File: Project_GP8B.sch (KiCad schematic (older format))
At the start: 15 parts, among them U1 74AHC05, U2 74AHC05, U3 74AHC1G04, U4 74AHC1G04, U5 74AHC05

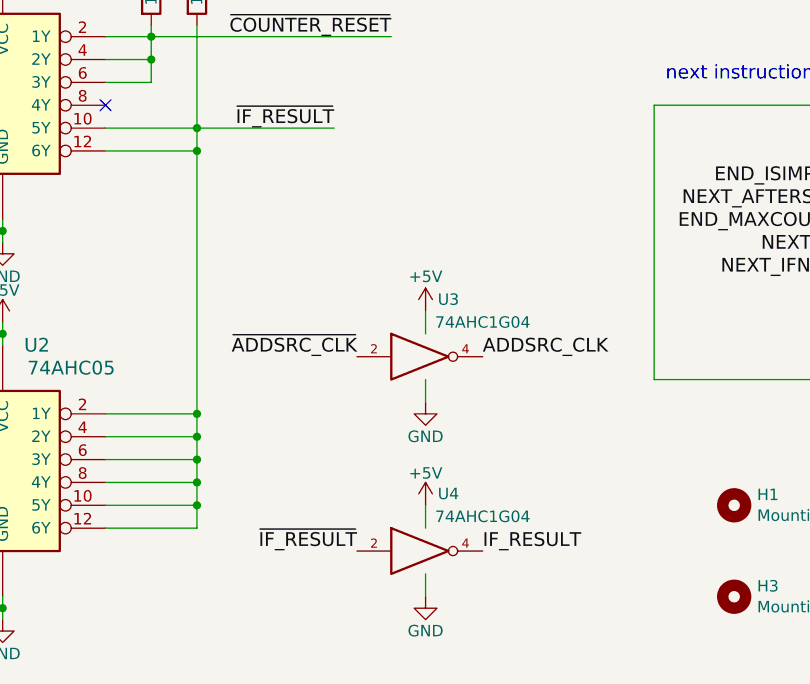
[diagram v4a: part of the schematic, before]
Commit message: Apply MM1 memory standard, and shared power pin symbol fix
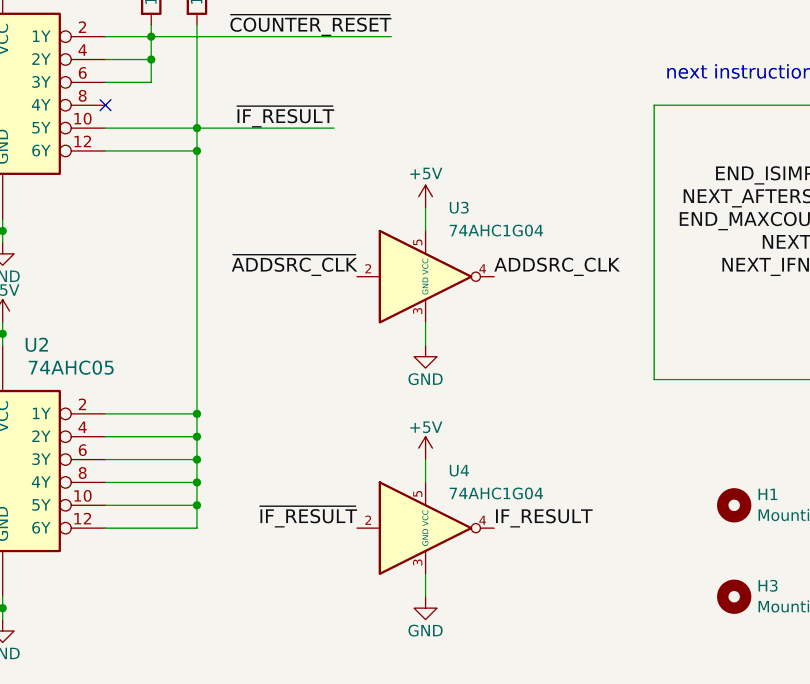
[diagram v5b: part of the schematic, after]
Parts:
- removed U3, U4: 74AHC1G04, Package_TO_SOT_SMD:SOT-23-5, symbol 74xGxx:74AHC1G04
- added U3, U4: 74AHC1G04, Package_TO_SOT_SMD:SOT-23-5, symbol Custom:74AHC1G04
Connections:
- net +5V: now also U3.5 (VCC), U4.5 (VCC)
- net ADDSRC_CLK: now also U3.4
- net GND: now also U3.3 (GND), U4.3 (GND)
- net IF_RESULT: now also U4.4
- net ~ADDSRC_CLK: now also U3.2
- net ~IF_RESULT: now also U4.2
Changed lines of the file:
@@
 L power:+5V #PWR07
 U 1 1 5B155C11
-P 3700 6150
-F 0 "#PWR07" H 3700 6000 50  0001 C CNN
-F 1 "+5V" H 3700 6300 50  0000 C CNN
-F 2 "" H 3700 6150 50  0001 C CNN
-F 3 "" H 3700 6150 50  0001 C CNN
-	1    3700 6150
+P 3700 5700
+F 0 "#PWR07" H 3700 5550 50  0001 C CNN
+F 1 "+5V" H 3700 5850 50  0000 C CNN
+F 2 "" H 3700 5700 50  0001 C CNN
+F 3 "" H 3700 5700 50  0001 C CNN
+	1    3700 5700
 	1    0    0    -1
 $EndComp
@@
 L power:+5V #PWR08
 U 1 1 5B15C5EC
-P 3700 7000
-F 0 "#PWR08" H 3700 6850 50  0001 C CNN
-F 1 "+5V" H 3700 7140 50  0000 C CNN
-F 2 "" H 3700 7000 50  0001 C CNN
-F 3 "" H 3700 7000 50  0001 C CNN
-	1    3700 7000
+P 3700 6800
+F 0 "#PWR08" H 3700 6650 50  0001 C CNN
+F 1 "+5V" H 3700 6940 50  0000 C CNN
+F 2 "" H 3700 6800 50  0001 C CNN
+F 3 "" H 3700 6800 50  0001 C CNN
+	1    3700 6800
 	1    0    0    -1
 $EndComp
@@
 L power:GND #PWR09
 U 1 1 5B15D182
-P 3700 6550
-F 0 "#PWR09" H 3700 6300 50  0001 C CNN
-F 1 "GND" H 3700 6400 50  0000 C CNN
-F 2 "" H 3700 6550 50  0001 C CNN
-F 3 "" H 3700 6550 50  0001 C CNN
-	1    3700 6550
+P 3700 6300
+F 0 "#PWR09" H 3700 6050 50  0001 C CNN
+F 1 "GND" H 3700 6150 50  0000 C CNN
+F 2 "" H 3700 6300 50  0001 C CNN
+F 3 "" H 3700 6300 50  0001 C CNN
+	1    3700 6300
 	1    0    0    -1
 $EndComp
@@
 	1    0    0    -1
 $EndComp
-Text Label 3400 7200 2    60   ~ 0
+Text Label 3400 7100 2    60   ~ 0
 ~IF_RESULT
-Text Label 3950 7200 0    60   ~ 0
+Text Label 4000 7100 0    60   ~ 0
 IF_RESULT
 Text Label 4900 800  2    60   ~ 0
@@
 	1    0    0    -1
 $EndComp
-$Comp
-L 74xGxx:74AHC1G04 U3
-U 1 1 5C94A9C5
-P 3700 6350
-F 0 "U3" H 3800 6600 50  0000 C CNN
-F 1 "74AHC1G04" H 3950 6500 50  0000 C CNN
-F 2 "Package_TO_SOT_SMD:SOT-23-5" H 3700 6350 50  0001 C CNN
-F 3 "http://www.ti.com/lit/sg/scyt129e/scyt129e.pdf" H 3700 6350 50  0001 C CNN
-	1    3700 6350
-	1    0    0    -1
-$EndComp
-Wire Wire Line
-	3700 6150 3700 6250
-Wire Wire Line
-	3700 6450 3700 6550
-$Comp
-L 74xGxx:74AHC1G04 U4
-U 1 1 5C971EB2
-P 3700 7200
-F 0 "U4" H 3800 7450 50  0000 C CNN
-F 1 "74AHC1G04" H 3950 7350 50  0000 C CNN
-F 2 "Package_TO_SOT_SMD:SOT-23-5" H 3700 7200 50  0001 C CNN
-F 3 "http://www.ti.com/lit/sg/scyt129e/scyt129e.pdf" H 3700 7200 50  0001 C CNN
-	1    3700 7200
-	1    0    0    -1
-$EndComp
-Wire Wire Line
-	3700 7000 3700 7100
+Wire Wire Line
+	3700 5700 3700 5800
+Wire Wire Line
+	3700 6200 3700 6300
+Wire Wire Line
+	3700 6800 3700 6900
 Wire Wire Line
 	3700 7300 3700 7400
@@
 Text Label 7250 5600 2    60   ~ 0
 ~ADDSRC_CLK
-Text Label 3400 6350 2    60   ~ 0
+Text Label 3400 6000 2    60   ~ 0
 ~ADDSRC_CLK
-Text Label 3950 6350 0    60   ~ 0
+Text Label 4000 6000 0    60   ~ 0
 ADDSRC_CLK
 $Sheet
@@
 F23 "SPI_CS" I L 1400 2350 60
 $EndSheet
+$Comp
+L Custom:74AHC1G04 U4
+U 1 1 5F3E18E2
+P 3700 7100
+F 0 "U4" H 3800 7350 50  0000 L CNN
+F 1 "74AHC1G04" H 3800 7250 50  0000 L CNN
+F 2 "Package_TO_SOT_SMD:SOT-23-5" H 3700 7100 50  0001 C CNN
+F 3 "https://assets.nexperia.com/documents/data-sheet/74AHC_AHCT1G04.pdf" H 3700 7100 50  0001 C CNN
+	1    3700 7100
+	1    0    0    -1
+$EndComp
+$Comp
+L Custom:74AHC1G04 U3
+U 1 1 5F3E1C89
+P 3700 6000
+F 0 "U3" H 3800 6300 50  0000 L CNN
+F 1 "74AHC1G04" H 3800 6200 50  0000 L CNN
+F 2 "Package_TO_SOT_SMD:SOT-23-5" H 3700 6000 50  0001 C CNN
+F 3 "https://assets.nexperia.com/documents/data-sheet/74AHC_AHCT1G04.pdf" H 3700 6000 50  0001 C CNN
+	1    3700 6000
+	1    0    0    -1
+$EndComp
 Wire Bus Line
 	1700 2800 1700 3600

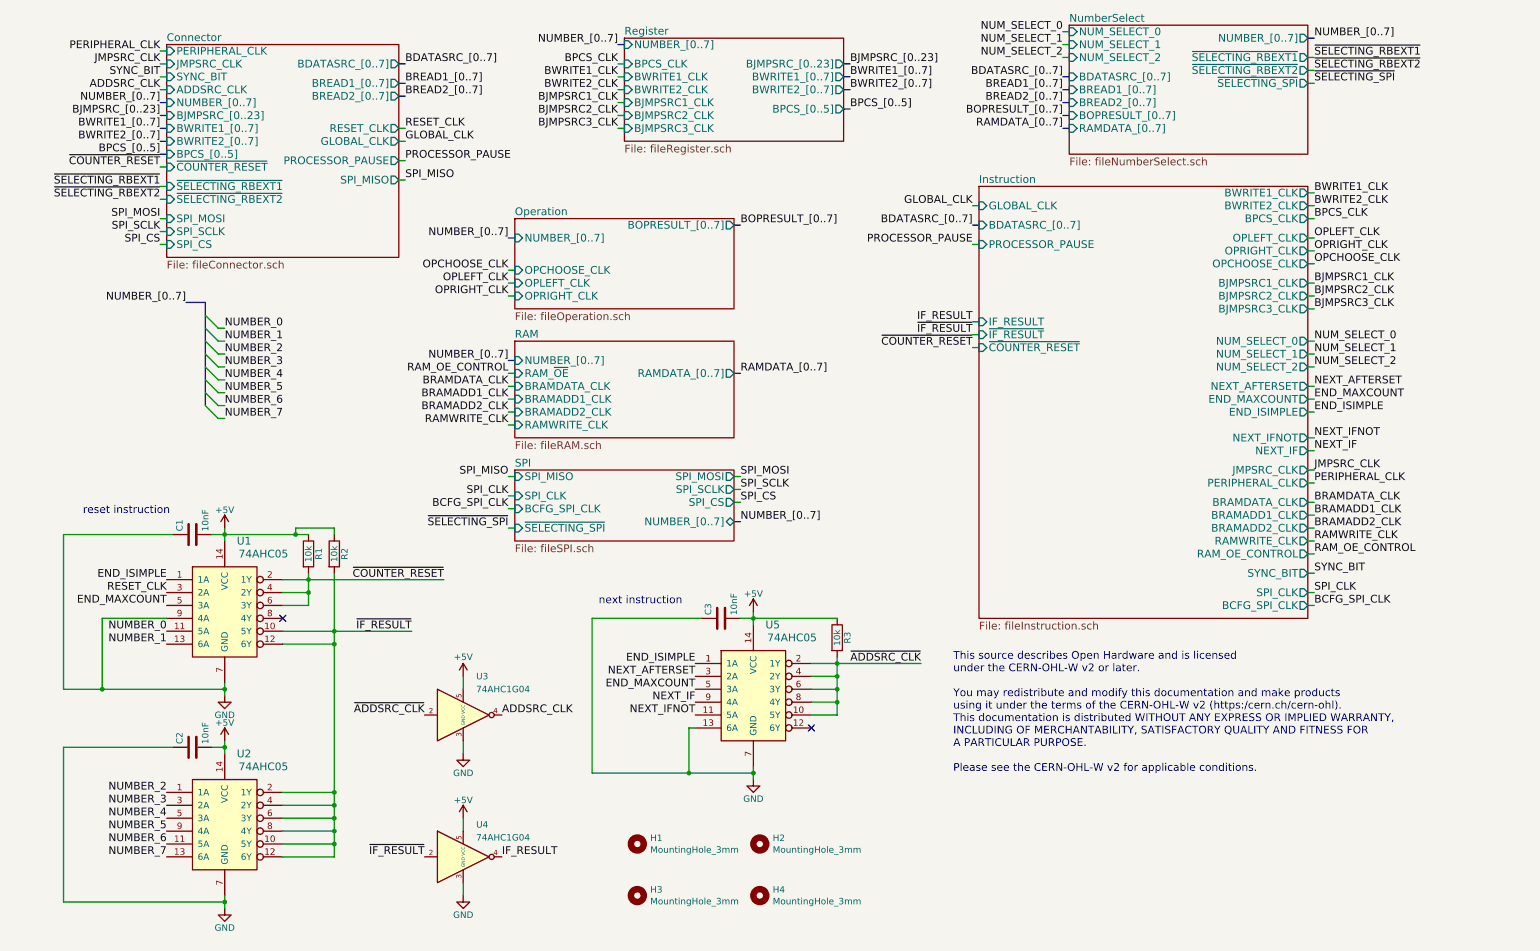
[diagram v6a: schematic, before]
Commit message: V5.1 (#9)
* Apply new symbol for XC2C256-VQ100 #5

* Set new date and 5.1

* Replacing 74HC165 with 74HC166, and add SPI_CFG_DS #4

* Replace some gates with a 74AHC1G02 to fix the pulse problem #3

* Go next only if SRCVALUE, (simple instruction)

* Remove weird ghost bus in register

* Small cleaning in fileRegister

* Go next only if SRCVALUE, (complex instruction) #8
adding 74AHC1G08

* Better decoupling #6

* Component association (#7)

* netlist

* Updated BOM for V5.1

* Routing, cleaning first pass

* bit of pcb cleaning

* SolderMaskClearance to 0

* Schematics to pdf

* PCB files in pdf

* exporting Gerbert files

* new 3d images

* Update README.md

* Modifying CHANGELOG file

* Update README.md
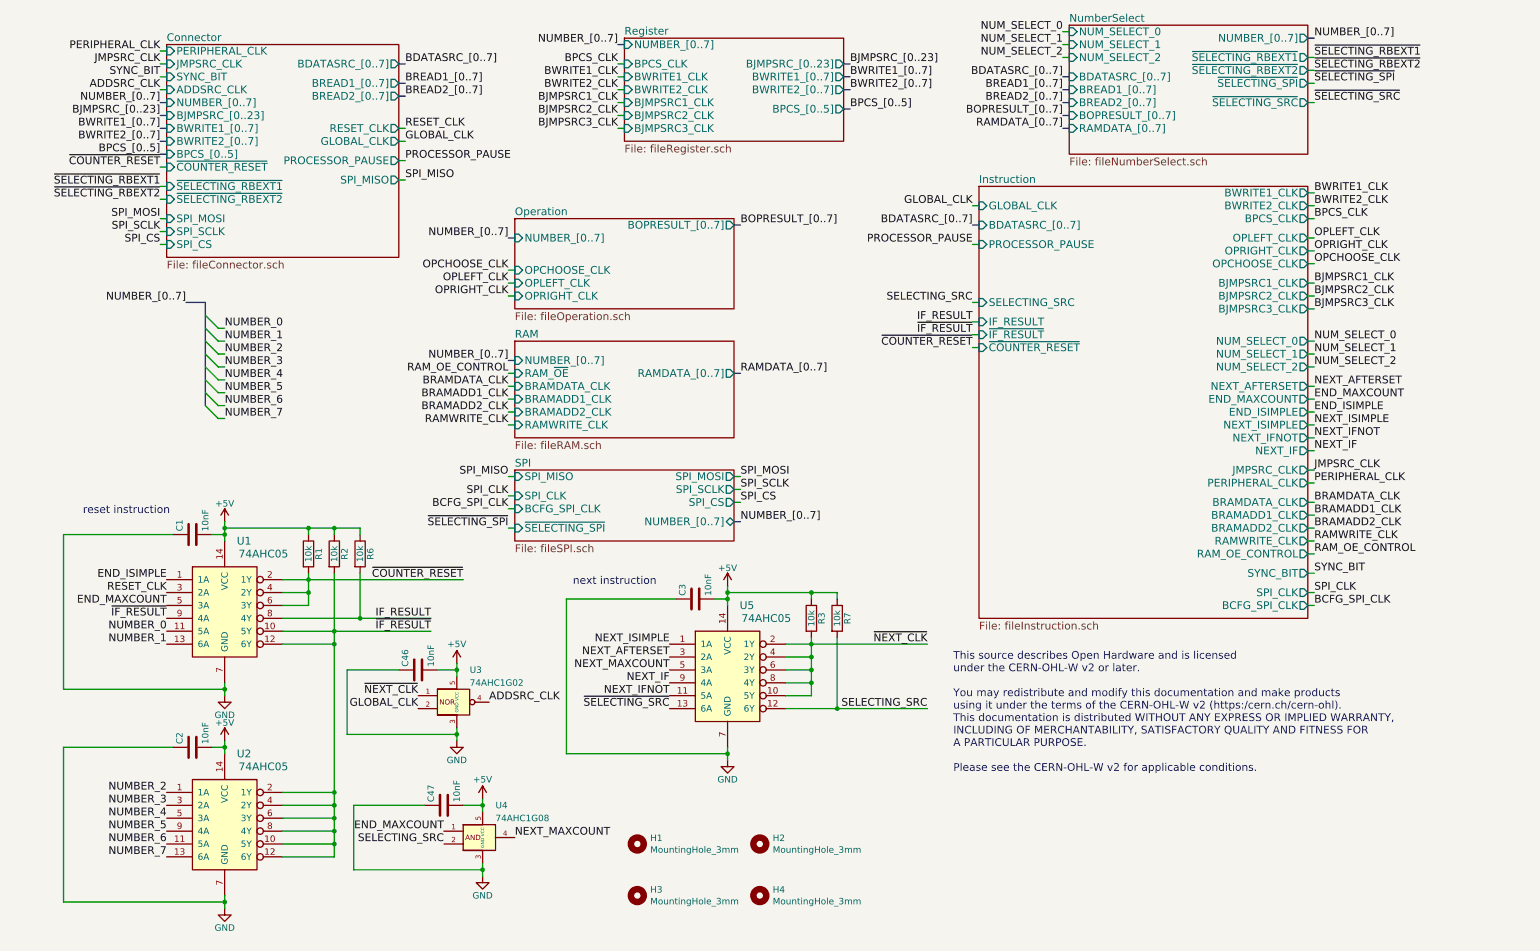
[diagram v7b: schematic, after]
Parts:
- removed U3, U4: 74AHC1G04, Package_TO_SOT_SMD:SOT-23-5, symbol Custom:74AHC1G04
- added C46, C47: 10nF, Capacitor_SMD:C_0805_2012Metric, symbol Device:C
- added R6, R7: 10k, Resistor_SMD:R_0805_2012Metric, symbol Device:R
- added U3: 74AHC1G02, Package_TO_SOT_SMD:SOT-23-5, symbol Custom:74AHC1G02
- added U4: 74AHC1G08, Package_TO_SOT_SMD:SOT-23-5, symbol Custom:74AHC1G08
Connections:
- net +5V: now also C46.2, C47.2, R6.1, R7.1, U3.5 (VCC), U4.5 (VCC)
- net ADDSRC_CLK: now also U3.4
- net END_ISIMPLE: no longer U5.1 (1A)
- net END_MAXCOUNT: now also U4.1; no longer U5.5 (3A)
- net GLOBAL_CLK: now also U3.2
- net GND: now also C46.1, C47.1, U3.3 (GND), U4.3 (GND); no longer U1.9 (4A), U5.13 (6A)
- net IF_RESULT: now also U1.8 (4Y), R6.2
- net ~IF_RESULT: now also U1.9 (4A)
- net SELECTING_SRC: now reaches U5.12 (6Y)
- net SELECTING_SRC: now also R7.2, U4.2
- net ~ADDSRC_CLK renamed ~NEXT_CLK
- net ~NEXT_CLK: now also U3.1
- new net NEXT_ISIMPLE: U5.1 (1A)
- new net NEXT_MAXCOUNT: U4.4, U5.5 (3A)
- new net ~SELECTING_SRC: U5.13 (6A)
- no-connect marks 2 -> 0
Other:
- moved on the sheet: C3, R3, U5
